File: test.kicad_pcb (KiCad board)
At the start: 2 copper layers, 63.5 x 38.1 mm, 42 parts, among them J1 Analog GPIO, J2 ICSP, J3 SPI, J4 UART, J5 USB4085-GF-A_REVA, J6 Digital GPIO, J7 I2C, J8 Power, SW1 Reset Button, U1 PIC32MX340F512H-80V_PT, U2 AZ1117EH-3.3TRG1, U3 AZ1117EH-5.0TRG1, Y1 Y

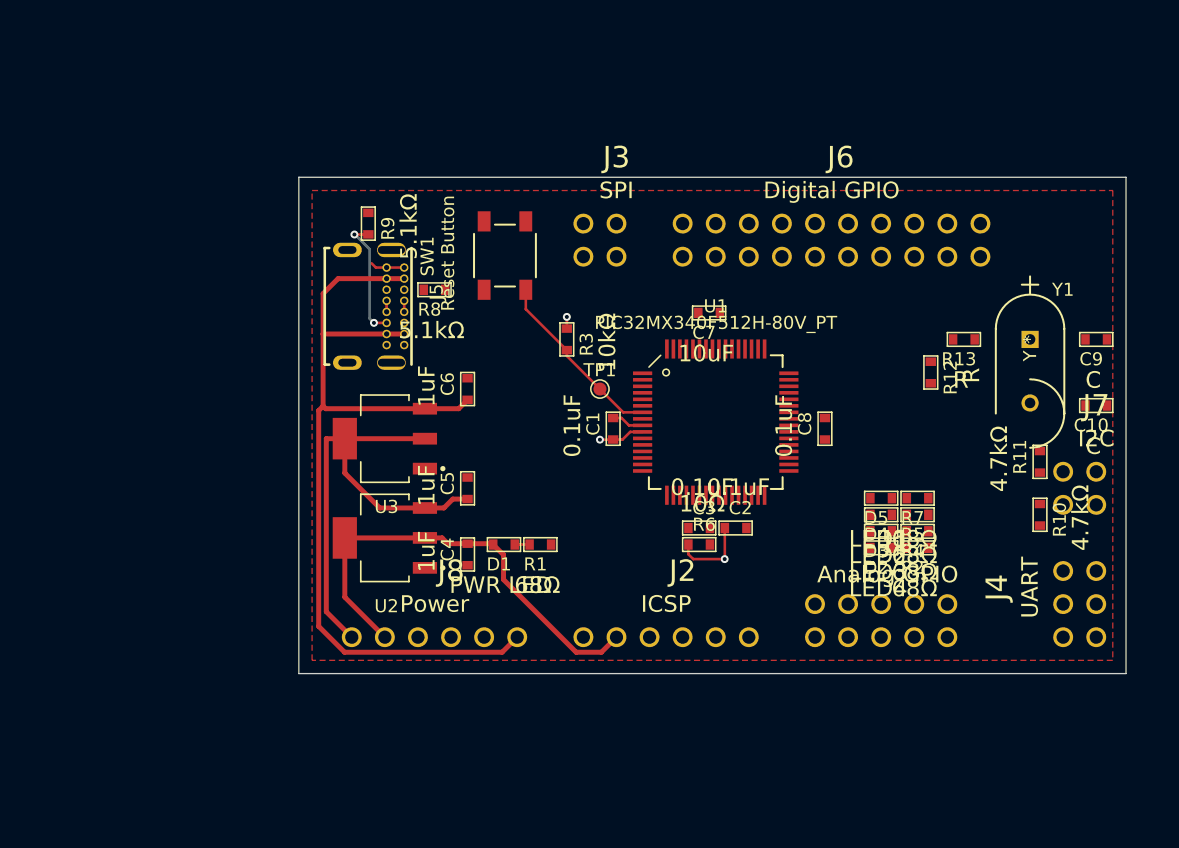
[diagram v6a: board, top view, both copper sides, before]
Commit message: Finished following changes... - Removed SMD test points for power and replaced with USB-C port - Added 2 voltage regulators for 5v and 3v3 - Added a 6 port power header for 5v, 3v3, GND, and VIN - Added a 10 port analog header - Shifted ICSP PGD and PGC pins from the 1st to 2nd set to allow for use of AN0 and AN1 which are also used for possible reference voltages for analog data - Added a crystal oscillator - Simplified MCLR circuit, think there was a lot more there than was necessary
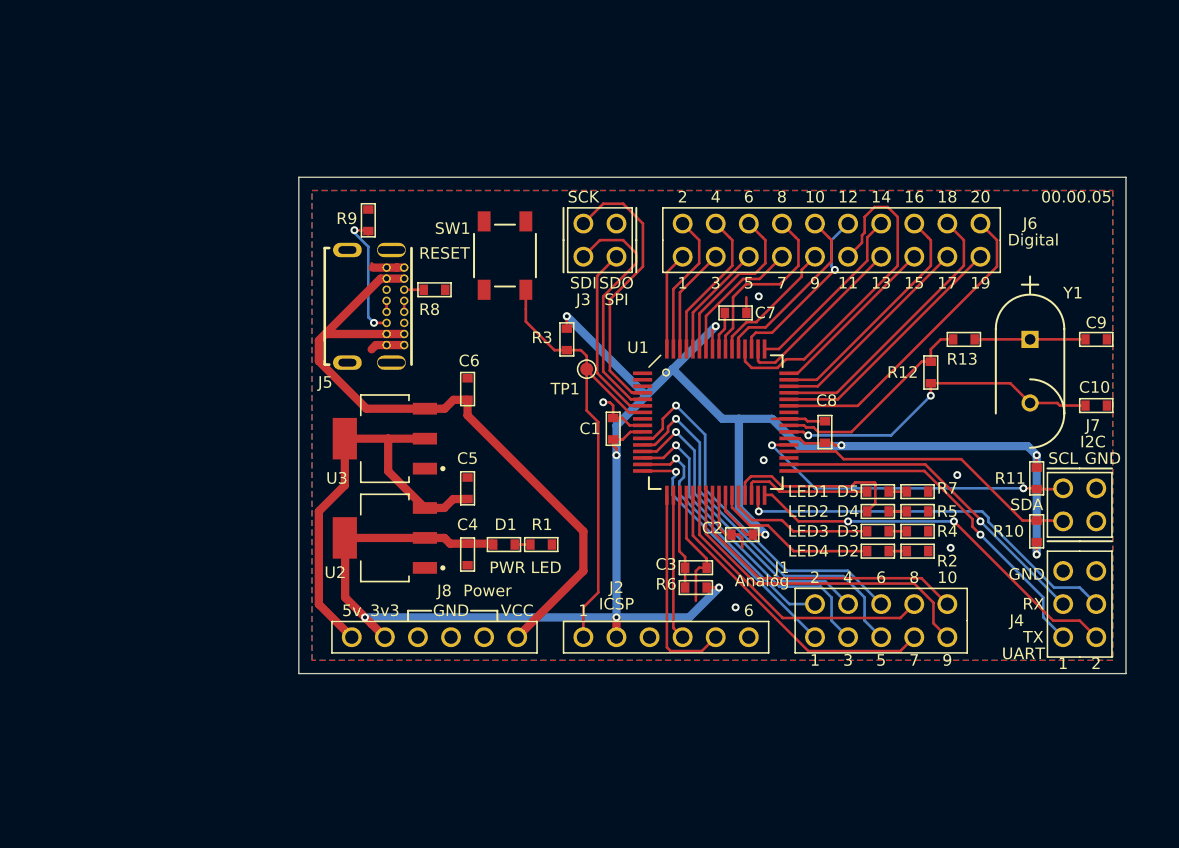
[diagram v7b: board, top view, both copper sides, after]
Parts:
- J1: value Analog GPIO -> Analog
- J6: value Digital GPIO -> Digital; footprint mod:02x20 -> mod:02x10
- moved R6 3.31 mm to (153.4, 114.3), turned to 180 degrees
- moved C3 3.06 mm to (153.4, 112.8), turned to 180 degrees
- moved C7 2.03 mm to (156.5, 93.2), turned to 0 degrees
- moved TP1 1.83 mm to (145.0, 97.5)
- moved R11 1.30 mm to (179.6, 105.9)
- moved R10 1.30 mm to (179.6, 110.0)
- moved J7 1.27 mm to (181.6, 106.7)
- moved C2 0.72 mm to (157.0, 110.2), turned to 180 degrees
- moved D5 0.57 mm to (167.4, 106.9)
- moved R7 0.51 mm to (170.4, 106.9)
- moved D2 0.36 mm to (167.4, 111.5)
- moved D4 0.36 mm to (167.4, 108.5)
- moved R2 0.25 mm to (170.4, 111.5)
- moved R5 0.25 mm to (170.4, 108.5)
- moved R9 0.25 mm to (128.3, 86.1)
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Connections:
- J3 pad 4: Net-(J3-Pad4) -> GNDREF
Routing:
- net +3V3: track 45.5 -> 151.2 mm, vias 3 -> 10
- net Net-(J4-Pad3): track 0.00 -> 30.3 mm, vias 0 -> 1
- net Net-(J4-Pad1): track 0.00 -> 30.0 mm, vias 0 -> 2
- net Net-(J1-Pad5): track 0.00 -> 29.5 mm, vias 0 -> 1
- net Net-(J1-Pad6): track 0.00 -> 28.6 mm, vias 0 -> 1
- net Net-(J4-Pad2): track 0.00 -> 27.6 mm, vias 0 -> 1
- net Net-(J6-Pad11): track 0.00 -> 27.5 mm
- net Net-(J4-Pad4): track 0.00 -> 25.9 mm, vias 0 -> 1
- net Net-(J1-Pad9): track 0.00 -> 25.8 mm
- net Net-(C10-Pad2): track 0.00 -> 25.8 mm, vias 0 -> 2
- net Net-(J1-Pad3): track 0.00 -> 25.0 mm, vias 0 -> 1
- net Net-(J7-Pad2): track 0.00 -> 25.0 mm, vias 0 -> 2
- net GNDREF: track 5.13 -> 30.0 mm, vias 0 -> 6
- net Net-(J6-Pad20): track 0.00 -> 24.2 mm
- net Net-(J1-Pad7): track 0.00 -> 24.2 mm
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- added copper zone on B.Cu, net GNDREF
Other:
- board text added: "00.00.05"
- board text added: "1"
- board text added: "10"
- board text added: "11"
- board text added: "12"
- board text added: "13"
- board text added: "14"
- board text added: "15"
- board text added: "16"
- board text added: "17"
- board text added: "18"
- board text added: "19"
- board text added: "2"
- board text added: "20"
- board text added: "3"
- board text added: "3v3"
- board text added: "4"
- board text added: "5"
- board text added: "5v"
- board text added: "6"
- board text added: "7"
- board text added: "8"
- board text added: "9"
- board text added: "GND"
- board text added: "RESET"
- board text added: "RX"
- board text added: "SCK"
- board text added: "SCL"
- board text added: "SDA"
- board text added: "SDI"
- board text added: "SDO"
- board text added: "TX"
- board text added: "VCC"
